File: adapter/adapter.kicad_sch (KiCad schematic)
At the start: 32 parts, among them J1 Serial, J10 Ribbon, J11 Ribbon, J12 Ribbon, J13 serial, J14 serial, J2 Serial, J3 battery charge, J4 RGB, J5 RGB, J6 battery charge, J7 trackball, J8 trackball, J9 Ribbon, SW1 SW_SPST, SW2 SW_SPST, SW3 SW_SPDT, SW4 SW_SPDT, U1 eliteC, U2 eliteC

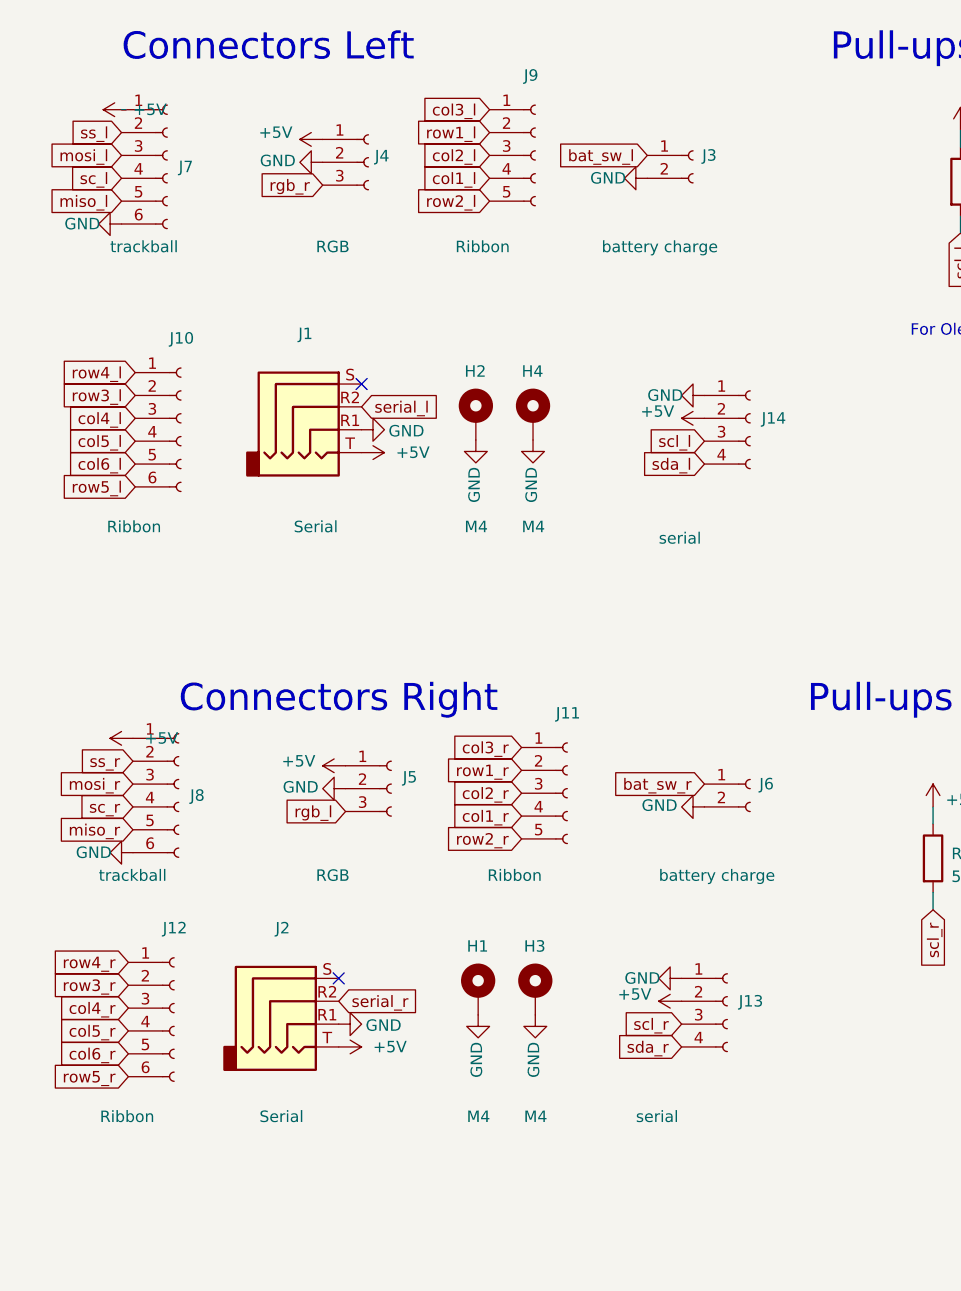
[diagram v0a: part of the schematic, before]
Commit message: initial work on rj9 mod
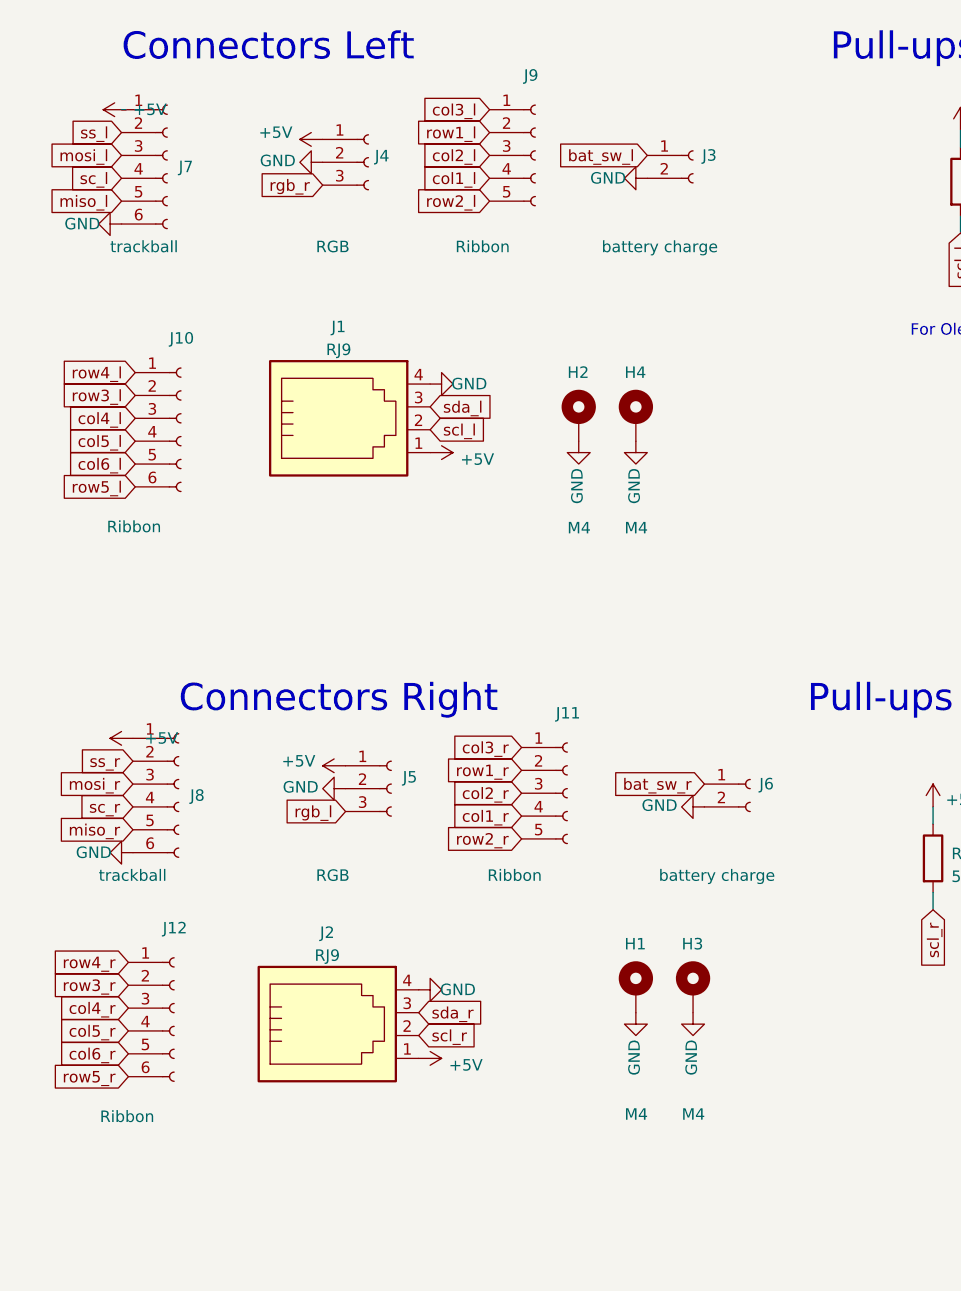
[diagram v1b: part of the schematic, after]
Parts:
- removed J1, J2: Serial, Library:Jack_3.5mm_PJ320E_Horizontal, symbol Connector:AudioJack4
- removed J13, J14: serial, Library:PinHeader_1x04_P2.54mm_Vertical, symbol Connector:Conn_01x04_Female
- added J1, J2: RJ9, JohnDeereLibrary:MOLEX_0955012401, symbol Connector:RJ9
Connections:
- net +5V: now also J1.1, J2.1
- net GND: now also J1.4, J2.4
- net scl_l: now also J1.2
- net scl_r: now also J2.2
- net sda_l: now also J1.3
- net sda_r: now also J2.3
- no-connect marks 10 -> 8
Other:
- moved on the sheet: H1, H2, H3, H4
